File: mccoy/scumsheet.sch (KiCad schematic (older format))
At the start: 12 parts, among them U8 scum3

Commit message: added back labels
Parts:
- removed C1, C14, C15, C16, C17, C18, C19, C20, C22, C24: NP, Capacitor_SMD:C_0402_1005Metric, symbol Device:C
- removed R13: NP, Resistor_SMD:R_0402_1005Metric, symbol Device:R_US
- added J10, J11, J12, J13, J14, J15, J16, J17, J18, J19, J4, J5, J6, J7, J8, J9: through_hole, SCUM:through_hole, symbol draft1library:through_hole
- renumbered U8 to U1
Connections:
- net +VDDD: no longer U1.72 (VDDD_LDO_OUTPUT)
- net at U1.1 (NC): now also J6.1 (pin)
- net at U1.100 (NC): now also J14.1 (pin)
- net PA_LDO_OUTPUT: now reaches U1.18 (PA_LDO_OUTPUT)
- net at U1.19 (STATIC_DIVIDER_OUTPUT): now also J11.1 (pin)
- net at U1.2 (NC): now also J7.1 (pin)
- net at U1.20 (MOD_IN): now also J12.1 (pin)
- net LO_LDO_OUTPUT: now reaches U1.22 (LO_LDO_OUTPUT)
- net at U1.23 (800mV_BANDGAP): now also J13.1 (pin)
- net at U1.3 (NC): now also J8.1 (pin)
- net at U1.56 (LF_CLK_EXT_IN): now also J17.1 (pin)
- net at U1.65 (ASC_OUT): now also J16.1 (pin)
- net at U1.67 (ASC_IN): now also J15.1 (pin)
- net at U1.7 (IF_DBG_OUT_QP): now also J9.1 (pin)
- net VDDD_DISABLE: now reaches U1.71 (VDDD_DISABLE)
- net at U1.73 (NC): now also J5.1 (pin)
- net at U1.75 (NC): now also J4.1 (pin)
- net at U1.8 (IF_DBG_IN_QN): now also J10.1 (pin)
- net at U1.96 (NC): now also J19.1 (pin)
- net at U1.98 (NC): now also J18.1 (pin)
- new net VDDD_LDO_OUTPUT: U1.72 (VDDD_LDO_OUTPUT)
- no-connect marks 50 -> 33

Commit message: updated with review material
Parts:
- added J?: through_hole, SCUM:through_hole, symbol draft1library:through_hole
- renumbered J4 to J20
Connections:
- net at U1.19 (STATIC_DIVIDER_OUTPUT): no longer J11.1 (pin)
- net at U1.20 (MOD_IN): now also J11.1 (pin); no longer J12.1 (pin)
- net at U1.21 (MOD_CLK_IN): now also J12.1 (pin)
- net GPO_ZERO: no longer names the net of U1.57 (GPO_ZERO)
- net GPO_ZERO: now also J?.1 (pin)
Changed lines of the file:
@@
 Wire Wire Line
 	5500 6050 5500 6500
-Wire Wire Line
-	8000 4650 9100 4650
-Text HLabel 9100 4650 2    50   BiDi ~ 0
-GPO_ZERO
 NoConn ~ 2250 3650
 NoConn ~ 2250 3200
@@
 	4850 1150 4850 700
 $Comp
-L draft1library:through_hole J4
+L draft1library:through_hole J20
 U 1 1 6090C006
 P 8000 1950
-F 0 "J4" H 8000 2150 50  0001 C CNN
+F 0 "J20" H 8000 2150 50  0001 C CNN
 F 1 "through_hole" H 8000 2050 50  0001 C CNN
 F 2 "SCUM:through_hole" H 8000 1950 50  0001 C CNN
@@
 L draft1library:through_hole J11
 U 1 1 609130FD
-P 2250 4700
-F 0 "J11" H 2250 4900 50  0001 C CNN
-F 1 "through_hole" H 2250 4800 50  0001 C CNN
-F 2 "SCUM:through_hole" H 2250 4700 50  0001 C CNN
-F 3 "" H 2250 4700 50  0001 C CNN
-	1    2250 4700
-	-1   0    0    1
-$EndComp
-$Comp
-L draft1library:through_hole J12
-U 1 1 60913103
 P 2250 4850
-F 0 "J12" H 2250 5050 50  0001 C CNN
+F 0 "J11" H 2250 5050 50  0001 C CNN
 F 1 "through_hole" H 2250 4950 50  0001 C CNN
 F 2 "SCUM:through_hole" H 2250 4850 50  0001 C CNN
@@
 	-1   0    0    1
 $EndComp
-NoConn ~ 2250 5000
+$Comp
+L draft1library:through_hole J12
+U 1 1 60913103
+P 2250 5000
+F 0 "J12" H 2250 5200 50  0001 C CNN
+F 1 "through_hole" H 2250 5100 50  0001 C CNN
+F 2 "SCUM:through_hole" H 2250 5000 50  0001 C CNN
+F 3 "" H 2250 5000 50  0001 C CNN
+	1    2250 5000
+	-1   0    0    1
+$EndComp
+NoConn ~ 2250 4700
 $Comp
 L draft1library:through_hole J8
@@
 	0    -1   -1   0
 $EndComp
+$Comp
+L draft1library:through_hole J?
+U 1 1 608F8296
+P 8000 4650
+F 0 "J?" H 8000 4850 50  0001 C CNN
+F 1 "through_hole" H 8000 4750 50  0001 C CNN
+F 2 "SCUM:through_hole" H 8000 4650 50  0001 C CNN
+F 3 "" H 8000 4650 50  0001 C CNN
+	1    8000 4650
+	1    0    0    -1
+$EndComp
 $EndSCHEMATC

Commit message: label a hole
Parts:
- gave numbers to parts that had none: 1
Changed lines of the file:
@@
 $EndComp
 $Comp
-L draft1library:through_hole J?
+L draft1library:through_hole J21
 U 1 1 608F8296
 P 8000 4650
-F 0 "J?" H 8000 4850 50  0001 C CNN
+F 0 "J21" H 8000 4850 50  0001 C CNN
 F 1 "through_hole" H 8000 4750 50  0001 C CNN
 F 2 "SCUM:through_hole" H 8000 4650 50  0001 C CNN

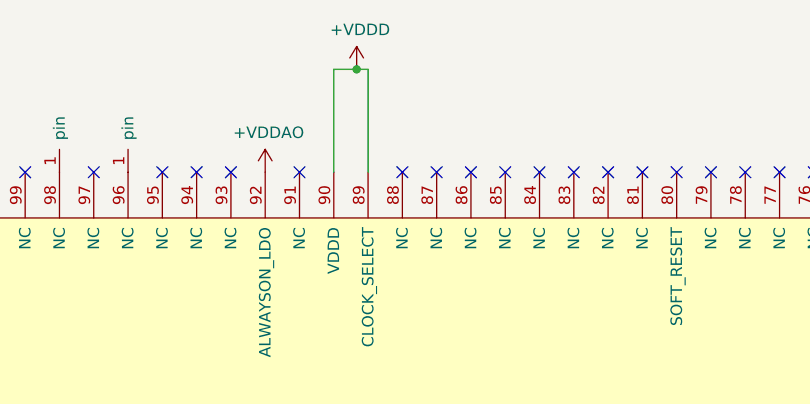
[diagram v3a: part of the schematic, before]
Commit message: added 0 ohm resistor footprint between pins 89 and 90
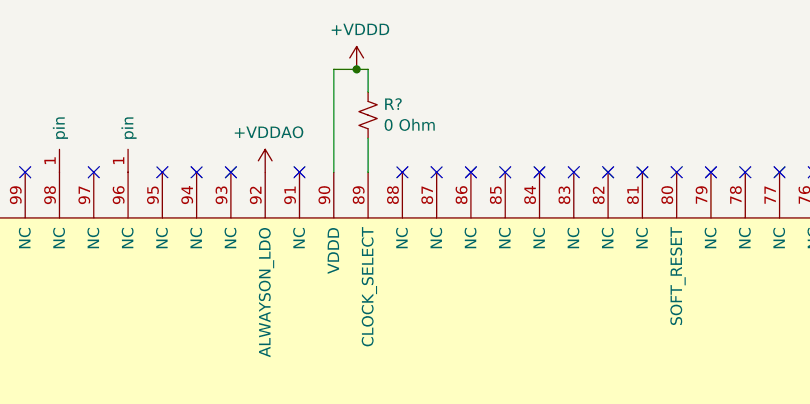
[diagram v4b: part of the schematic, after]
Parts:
- added R?: 0 Ohm, symbol Device:R_Small_US
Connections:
- net +VDDD: now also R?.1; no longer U1.89 (CLOCK_SELECT)
- new net: R?.2, U1.89 (CLOCK_SELECT)
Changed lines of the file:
@@
 	4950 700  4850 700
-Wire Wire Line
-	5000 700  5000 1150
 Wire Wire Line
 	4850 1150 4850 700
@@
 	1    0    0    -1
 $EndComp
+$Comp
+L Device:R_Small_US R?
+U 1 1 61298275
+P 5000 900
+F 0 "R?" H 5068 946 50  0000 L CNN
+F 1 "0 Ohm" H 5068 855 50  0000 L CNN
+F 2 "" H 5000 900 50  0001 C CNN
+F 3 "~" H 5000 900 50  0001 C CNN
+	1    5000 900
+	1    0    0    -1
+$EndComp
+Wire Wire Line
+	5000 700  5000 800
+Wire Wire Line
+	5000 1000 5000 1150
 $EndSCHEMATC
